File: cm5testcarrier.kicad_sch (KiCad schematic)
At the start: 48 parts, among them J1 Disable Bluetooth/Wifi, J10 HEADER-3X04, J11 HEADER-3X04, J12 HEADER-3X04, J13 Conn_02x20_Odd_Even, J14 GSB3112311HR, J16 TF38-22S-0.5SV_830_, J17 TF38-22S-0.5SV_830_, J2 GSB191217FHR, J3 ARJM11B1-502-NN-EW2, J4 GTFP08432B1HR, J5 Fan_Header, J6 Wago connector 2091-1372, J7 Wago connector 2091-1372, J8 Wago connector 2091-1372, J9 HEADER-3X04, U2 RT9742GGJ5, U3 AP22653W6-7, U4 PCA9685PW,118

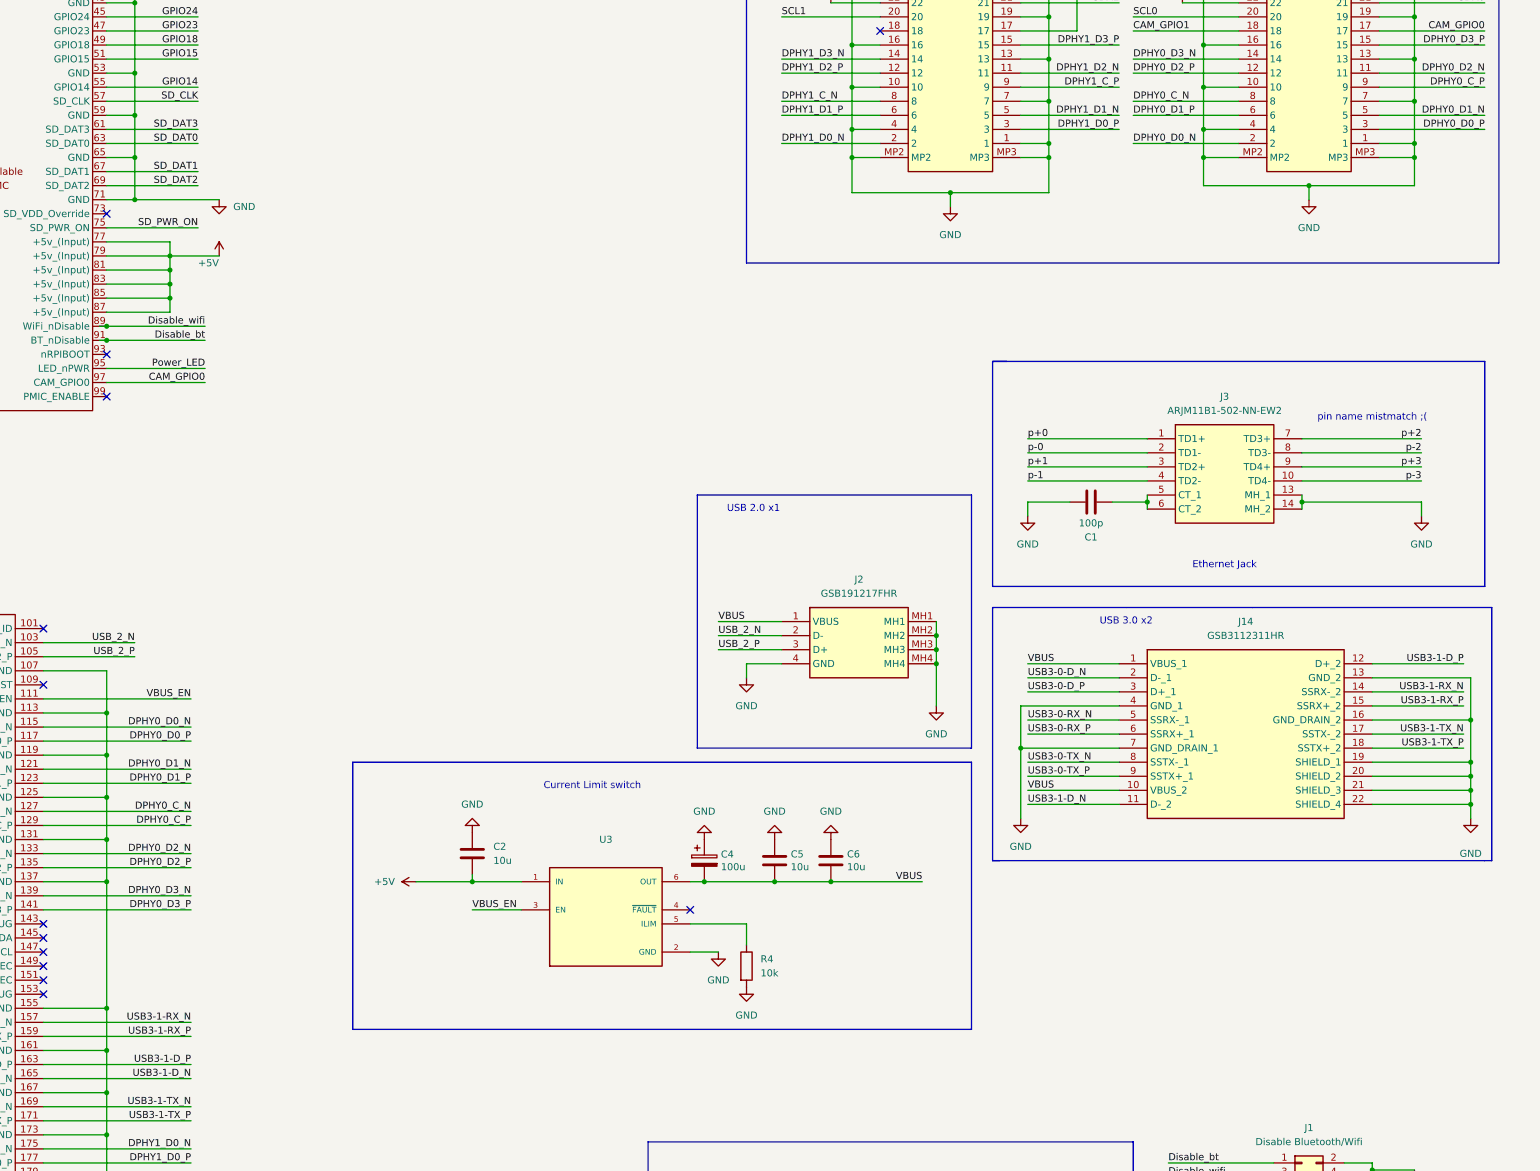
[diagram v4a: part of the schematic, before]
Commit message: V1 Done
- finished routing traces
- filled ground planes
- started readme documentation
- resized power traces for power needs
- relocated the servo setup to allow for better placement of the GPIO
- relocated some ports for better diff pair routing
- swapped cm5 board orientation for better routing (also doesn't matter because wireless will be unused)
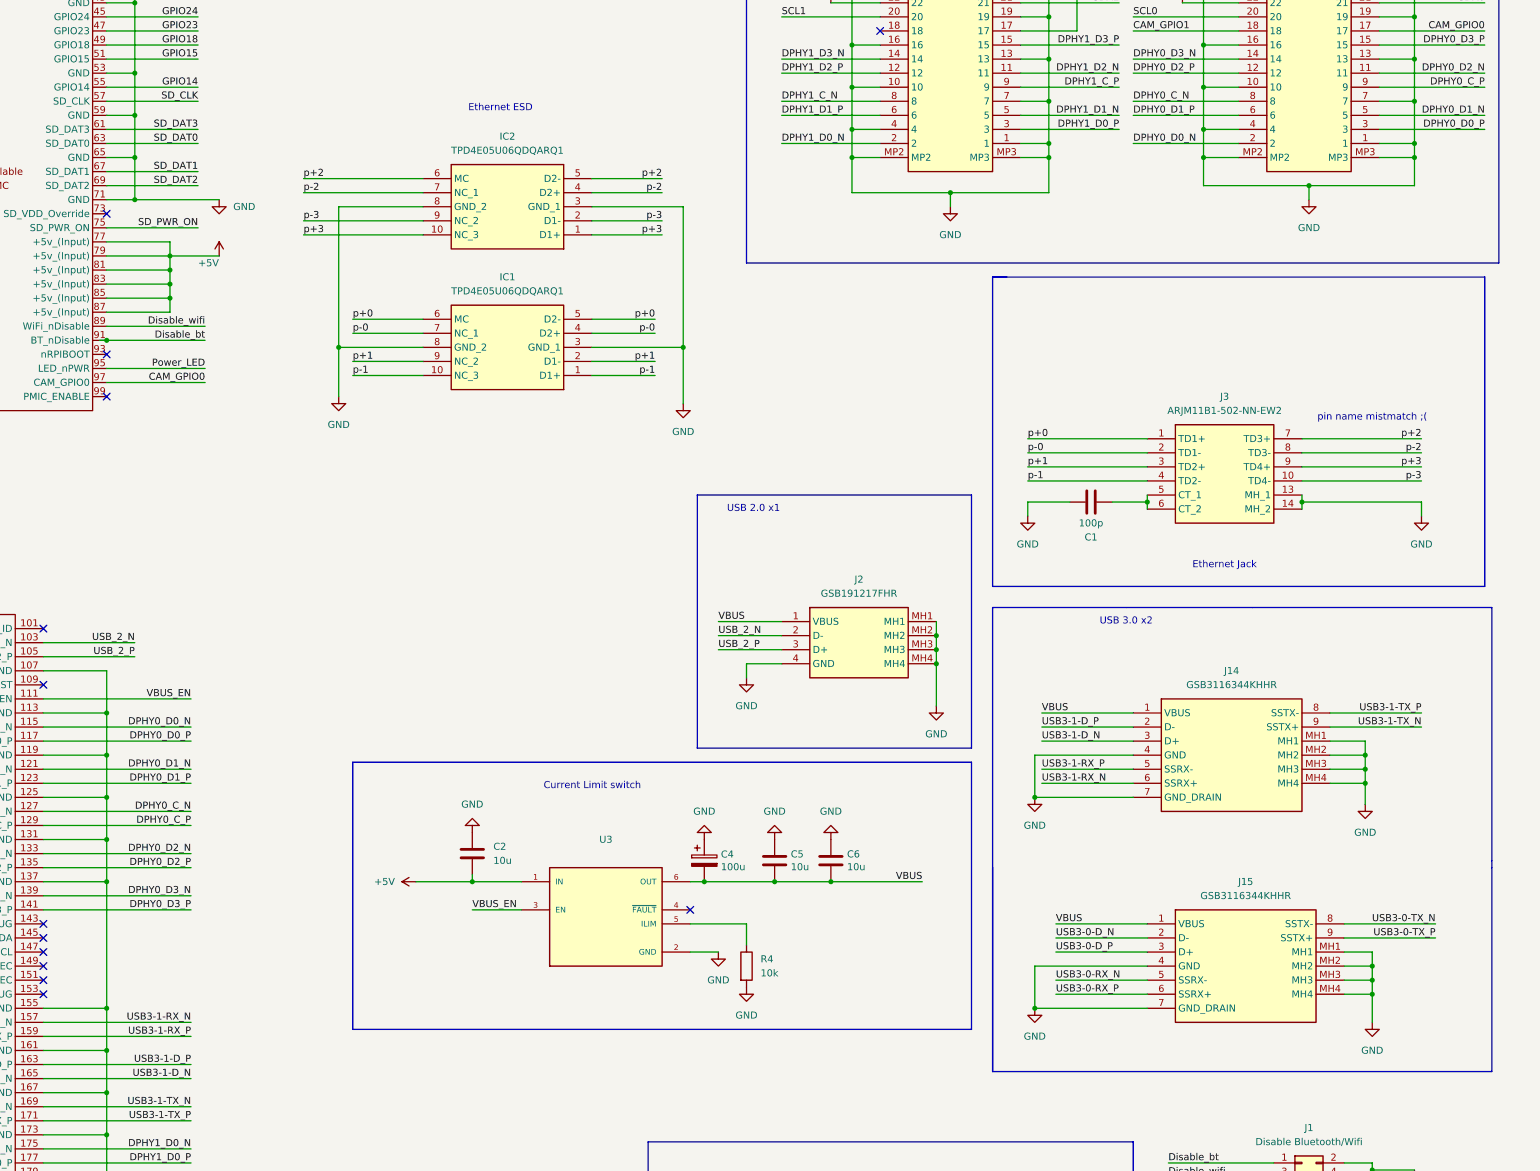
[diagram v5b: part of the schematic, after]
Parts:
- removed J14: GSB3112311HR, SamacSys_Parts:GSB3112311HR, symbol SamacSys_Parts:GSB3112311HR
- added IC1, IC2: TPD4E05U06QDQARQ1, SamacSys_Parts:DQA_R-PUSON-N10_, symbol SamacSys_Parts:TPD4E05U06QDQARQ1
- added J14, J15: GSB3116344KHHR, GSB3116344KHHR, symbol SamacSys_Parts:GSB3116344KHHR
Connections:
- net GND: now also IC1.3 (GND_1), IC1.8 (GND_2), IC2.3 (GND_1), IC2.8 (GND_2), J14.4 (GND), J14.7 (GND_DRAIN), J14.MH1, J14.MH2, J14.MH3, J14.MH4, J15.4 (GND), J15.7 (GND_DRAIN), J15.MH1, J15.MH2, J15.MH3, J15.MH4
- net USB3-0-D_N: now also J15.2 (D-)
- net USB3-0-D_P: now also J15.3 (D+)
- net USB3-0-RX_N: now also J15.5 (SSRX-)
- net USB3-0-RX_P: now also J15.6 (SSRX+)
- net USB3-0-TX_N: now also J15.8 (SSTX-)
- net USB3-0-TX_P: now also J15.9 (SSTX+)
- net USB3-1-D_N: now also J14.3 (D+)
- net USB3-1-D_P: now also J14.2 (D-)
- net USB3-1-RX_N: now also J14.6 (SSRX+)
- net USB3-1-RX_P: now also J14.5 (SSRX-)
- net USB3-1-TX_N: now also J14.9 (SSTX+)
- net USB3-1-TX_P: now also J14.8 (SSTX-)
- net VBUS: now also J14.1 (VBUS), J15.1 (VBUS)
- net p+0: now also IC1.5 (D2-), IC1.6 (MC)
- net p+1: now also IC1.2 (D1-), IC1.9 (NC_2)
- net p+2: now also IC2.5 (D2-), IC2.6 (MC)
- net p+3: now also IC2.1 (D1+), IC2.10 (NC_3)
- net p-0: now also IC1.4 (D2+), IC1.7 (NC_1)
- net p-1: now also IC1.1 (D1+), IC1.10 (NC_3)
- net p-2: now also IC2.4 (D2+), IC2.7 (NC_1)
- net p-3: now also IC2.2 (D1-), IC2.9 (NC_2)
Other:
- note added: "Ethernet ESD"
